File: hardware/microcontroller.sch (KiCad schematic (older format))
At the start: 13 parts, among them U8 STM32F411CEUx, Y1 12MHz

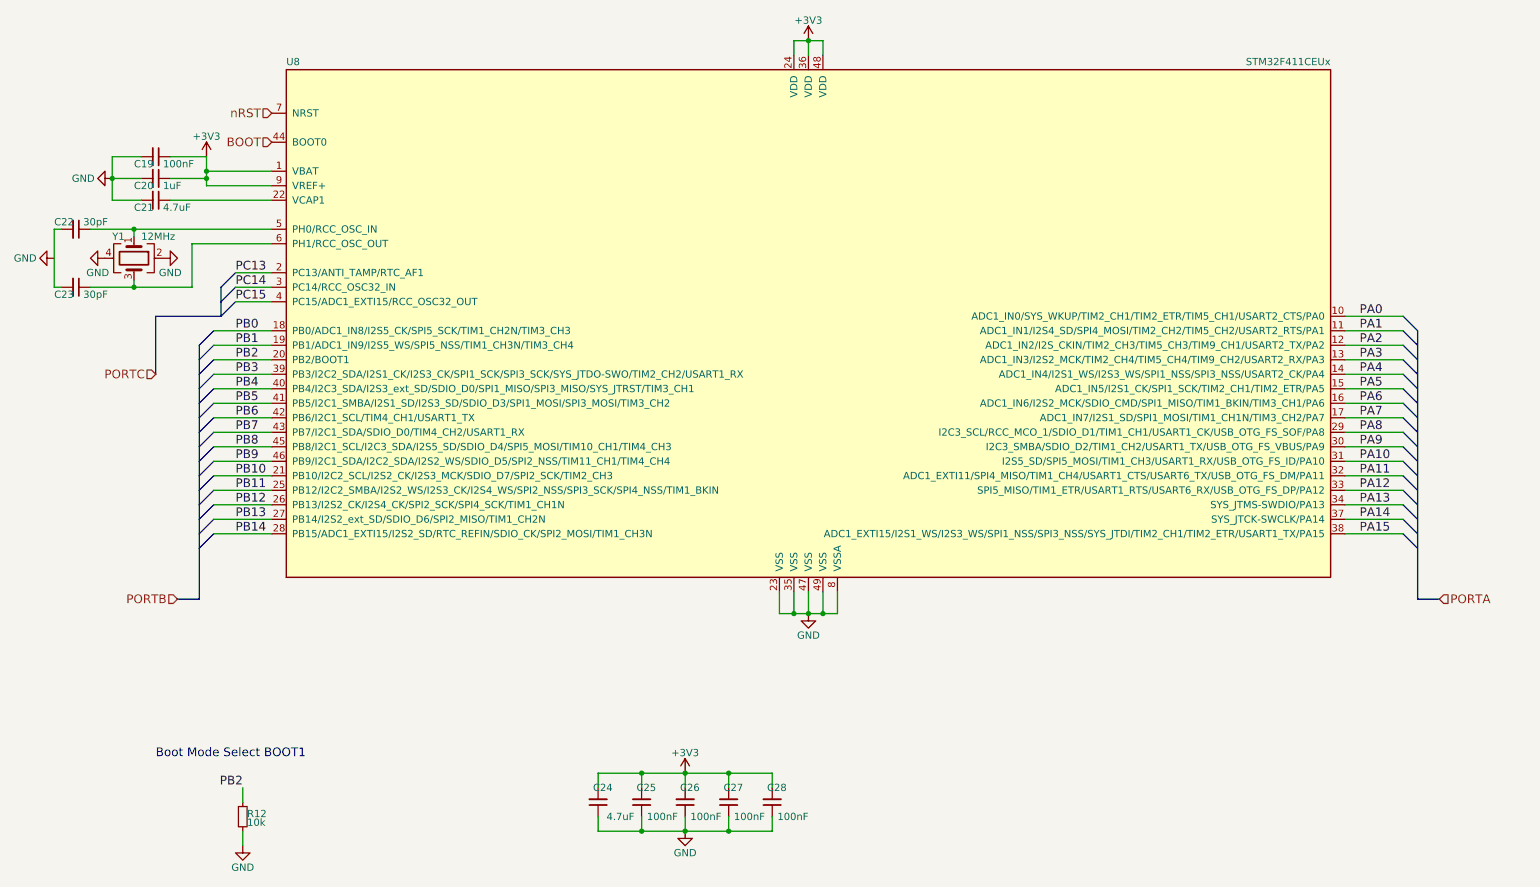
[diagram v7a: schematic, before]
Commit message: Start laying out the components for the PCB
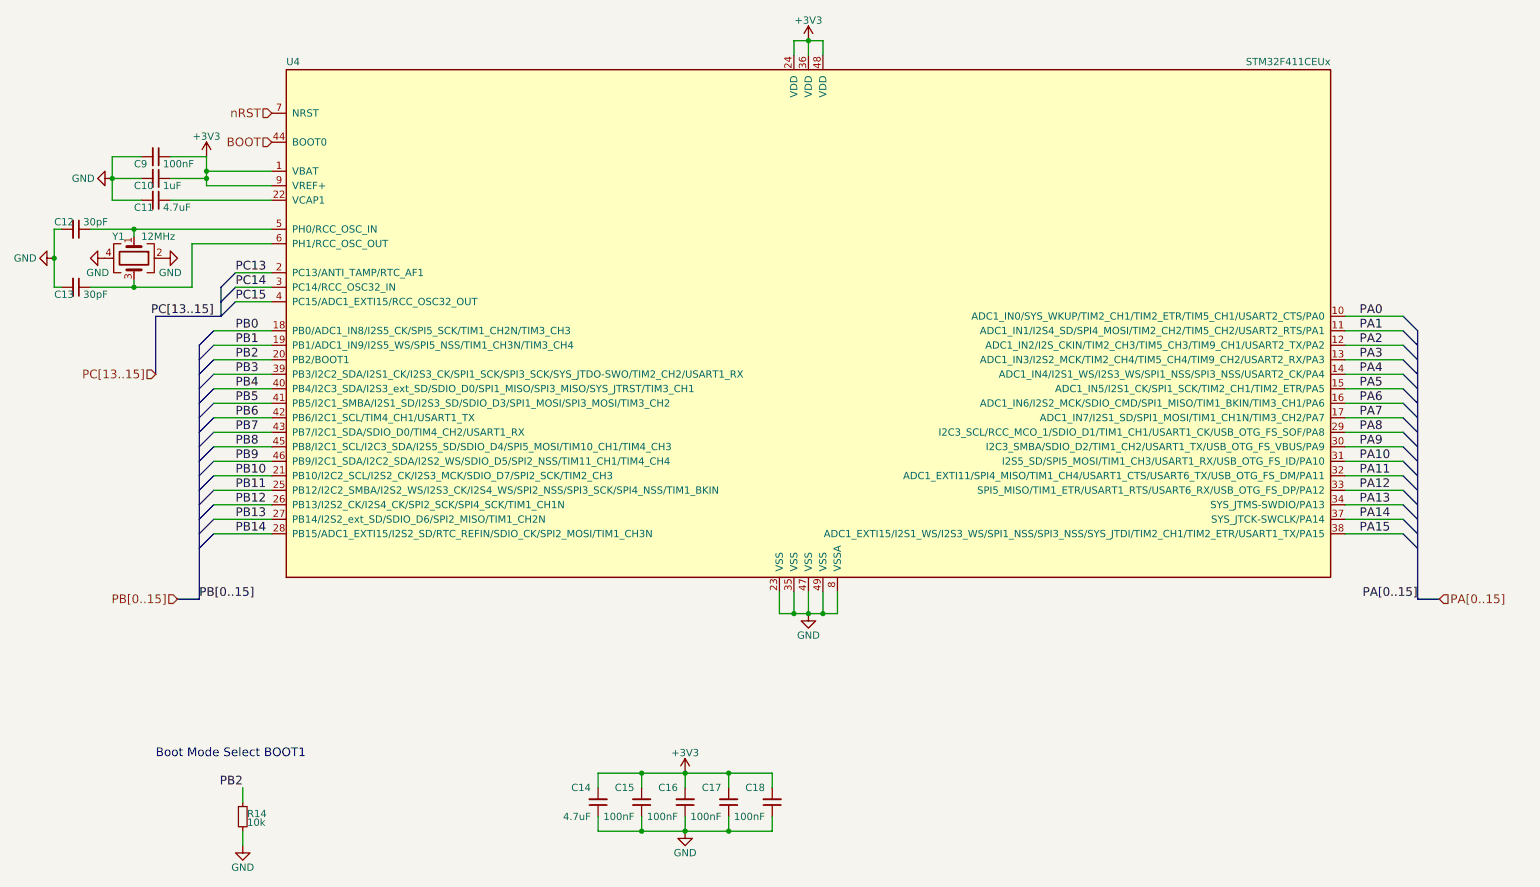
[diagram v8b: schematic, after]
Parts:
- Y1: footprint Crystals:Crystal_SMD_2520-4pin_2.5x2.0mm -> Crystals:Crystal_SMD_3225-4pin_3.2x2.5mm
- renumbered C20 to C10, C21 to C11, C22 to C12, C23 to C13, C24 to C14, C25 to C15, C26 to C16, C27 to C17, C28 to C18, C19 to C9, R12 to R14, U8 to U4
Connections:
- net labels added: PA[0..15], PB[0..15], PC[13..15]
- net labels removed: PORTA, PORTB, PORTC
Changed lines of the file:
@@
 encoding utf-8
 Sheet 2 2
-Title ""
-Date ""
-Rev ""
+Title "MiniBot"
+Date "2017-06-23"
+Rev "1"
 Comp ""
-Comment1 ""
+Comment1 "Ben Mitchell"
 Comment2 ""
 Comment3 ""
@@
 P 6000 3400
 AR Path="/59427B10" Ref="U?"  Part="1"
-AR Path="/59425D39/59427B10" Ref="U8"  Part="1"
-F 0 "U8" H 2400 5225 50  0000 L BNN
+AR Path="/59425D39/59427B10" Ref="U4"  Part="1"
+F 0 "U4" H 2400 5225 50  0000 L BNN
 F 1 "STM32F411CEUx" H 9600 5225 50  0000 R BNN
 F 2 "Housings_DFN_QFN:QFN-48-1EP_7x7mm_Pitch0.5mm" H 9600 5175 50  0001 R TNN
@@
 $EndComp
 $Comp
-L C_Small C21
+L C_Small C11
 U 1 1 59427B23
 P 1500 2500
-F 0 "C21" V 1550 2350 50  0000 L CNN
+F 0 "C11" V 1550 2350 50  0000 L CNN
 F 1 "4.7uF" V 1550 2550 50  0000 L CNN
 F 2 "Capacitors_SMD:C_0805" H 1500 2500 50  0001 C CNN
@@
 $EndComp
 $Comp
-L GND #PWR65
+L GND #PWR040
 U 1 1 59427B2A
 P 1200 2350
-F 0 "#PWR65" H 1200 2100 50  0001 C CNN
+F 0 "#PWR040" H 1200 2100 50  0001 C CNN
 F 1 "GND" V 1200 2150 50  0000 C CNN
 F 2 "" H 1200 2350 50  0001 C CNN
@@
 $EndComp
 $Comp
-L GND #PWR69
+L GND #PWR041
 U 1 1 59427B30
 P 6000 5350
-F 0 "#PWR69" H 6000 5100 50  0001 C CNN
+F 0 "#PWR041" H 6000 5100 50  0001 C CNN
 F 1 "GND" H 6000 5200 50  0000 C CNN
 F 2 "" H 6000 5350 50  0001 C CNN
@@
 $EndComp
 $Comp
-L C_Small C20
+L C_Small C10
 U 1 1 59427B36
 P 1500 2350
-F 0 "C20" V 1550 2200 50  0000 L CNN
+F 0 "C10" V 1550 2200 50  0000 L CNN
 F 1 "1uF" V 1550 2400 50  0000 L CNN
 F 2 "Capacitors_SMD:C_0805" H 1500 2350 50  0001 C CNN
@@
 $EndComp
 $Comp
-L C_Small C19
+L C_Small C9
 U 1 1 59427B3D
 P 1500 2200
-F 0 "C19" V 1550 2050 50  0000 L CNN
+F 0 "C9" V 1550 2050 50  0000 L CNN
 F 1 "100nF" V 1550 2250 50  0000 L CNN
 F 2 "Capacitors_SMD:C_0603" H 1500 2200 50  0001 C CNN
@@
 $EndComp
 $Comp
-L C_Small C25
+L C_Small C15
 U 1 1 59427B44
 P 4850 6650
-F 0 "C25" H 4750 6550 50  0000 L CNN
-F 1 "100nF" H 4600 6750 50  0000 L CNN
+F 0 "C15" H 4900 6550 50  0000 L CNN
+F 1 "100nF" H 4900 6750 50  0000 L CNN
 F 2 "Capacitors_SMD:C_0603" H 4850 6650 50  0001 C CNN
 F 3 "" H 4850 6650 50  0001 C CNN
@@
 $EndComp
 $Comp
-L C_Small C26
+L C_Small C16
 U 1 1 59427B4B
 P 5150 6650
-F 0 "C26" H 5050 6550 50  0000 L CNN
-F 1 "100nF" H 4900 6750 50  0000 L CNN
+F 0 "C16" H 5200 6550 50  0000 L CNN
+F 1 "100nF" H 5200 6750 50  0000 L CNN
 F 2 "Capacitors_SMD:C_0603" H 5150 6650 50  0001 C CNN
 F 3 "" H 5150 6650 50  0001 C CNN
@@
 $EndComp
 $Comp
-L C_Small C27
+L C_Small C17
 U 1 1 59427B52
 P 5450 6650
-F 0 "C27" H 5350 6550 50  0000 L CNN
-F 1 "100nF" H 5200 6750 50  0000 L CNN
+F 0 "C17" H 5500 6550 50  0000 L CNN
+F 1 "100nF" H 5500 6750 50  0000 L CNN
 F 2 "Capacitors_SMD:C_0603" H 5450 6650 50  0001 C CNN
 F 3 "" H 5450 6650 50  0001 C CNN
@@
 $EndComp
 $Comp
-L C_Small C28
+L C_Small C18
 U 1 1 59427B59
 P 5750 6650
-F 0 "C28" H 5650 6550 50  0000 L CNN
-F 1 "100nF" H 5500 6750 50  0000 L CNN
+F 0 "C18" H 5800 6550 50  0000 L CNN
+F 1 "100nF" H 5800 6750 50  0000 L CNN
 F 2 "Capacitors_SMD:C_0603" H 5750 6650 50  0001 C CNN
 F 3 "" H 5750 6650 50  0001 C CNN
@@
 $EndComp
 $Comp
-L GND #PWR71
+L GND #PWR042
 U 1 1 59427B60
 P 5150 6850
-F 0 "#PWR71" H 5150 6600 50  0001 C CNN
+F 0 "#PWR042" H 5150 6600 50  0001 C CNN
 F 1 "GND" H 5150 6700 50  0000 C CNN
 F 2 "" H 5150 6850 50  0001 C CNN
@@
 $EndComp
 $Comp
-L C_Small C24
+L C_Small C14
 U 1 1 59427B6C
 P 4550 6650
-F 0 "C24" H 4450 6550 50  0000 L CNN
-F 1 "4.7uF" H 4300 6750 50  0000 L CNN
+F 0 "C14" H 4600 6550 50  0000 L CNN
+F 1 "4.7uF" H 4600 6750 50  0000 L CNN
 F 2 "Capacitors_SMD:C_0805" H 4550 6650 50  0001 C CNN
 F 3 "" H 4550 6650 50  0001 C CNN
@@
 F 0 "Y1" V 1200 2750 50  0000 L CNN
 F 1 "12MHz" V 1200 2950 50  0000 L CNN
-F 2 "Crystals:Crystal_SMD_2520-4pin_2.5x2.0mm" H 1350 2900 50  0001 C CNN
+F 2 "Crystals:Crystal_SMD_3225-4pin_3.2x2.5mm" H 1350 2900 50  0001 C CNN
 F 3 "" H 1350 2900 50  0001 C CNN
 	1    1350 2900
@@
 Connection ~ 1350 3100
 $Comp
-L GND #PWR67
+L GND #PWR043
 U 1 1 59427C13
 P 1150 2900
-F 0 "#PWR67" H 1150 2650 50  0001 C CNN
+F 0 "#PWR043" H 1150 2650 50  0001 C CNN
 F 1 "GND" V 1250 2850 50  0000 C CNN
 F 2 "" H 1150 2900 50  0001 C CNN
@@
 $EndComp
 $Comp
-L GND #PWR68
+L GND #PWR044
 U 1 1 59427C19
 P 1550 2900
-F 0 "#PWR68" H 1550 2650 50  0001 C CNN
+F 0 "#PWR044" H 1550 2650 50  0001 C CNN
 F 1 "GND" V 1450 2850 50  0000 C CNN
 F 2 "" H 1550 2900 50  0001 C CNN
@@
 $EndComp
 $Comp
-L C_Small C23
+L C_Small C13
 U 1 1 59427C1F
 P 950 3100
-F 0 "C23" V 1000 2950 50  0000 L CNN
+F 0 "C13" V 1000 2950 50  0000 L CNN
 F 1 "30pF" V 1000 3150 50  0000 L CNN
 F 2 "Capacitors_SMD:C_0402" H 950 3100 50  0001 C CNN
@@
 	1750 3100 1050 3100
 $Comp
-L C_Small C22
+L C_Small C12
 U 1 1 59427C28
 P 950 2700
-F 0 "C22" V 900 2550 50  0000 L CNN
+F 0 "C12" V 900 2550 50  0000 L CNN
 F 1 "30pF" V 900 2750 50  0000 L CNN
 F 2 "Capacitors_SMD:C_0402" H 950 2700 50  0001 C CNN
@@
 	1050 2700 2300 2700
 $Comp
-L GND #PWR66
+L GND #PWR045
 U 1 1 59427C31
 P 800 2900
-F 0 "#PWR66" H 800 2650 50  0001 C CNN
+F 0 "#PWR045" H 800 2650 50  0001 C CNN
 F 1 "GND" V 800 2700 50  0000 C CNN
 F 2 "" H 800 2900 50  0001 C CNN
@@
 $EndComp
 Text HLabel 10350 5250 2    60   Input ~ 0
-PORTA
+PA[0..15]
 Text HLabel 1650 5250 0    60   Input ~ 0
-PORTB
+PB[0..15]
 Text HLabel 2300 1900 0    60   Input ~ 0
 nRST
@@
 PB2
 $Comp
-L R_Small R12
+L R_Small R14
 U 1 1 594293DA
 P 2100 6750
-F 0 "R12" H 2130 6770 50  0000 L CNN
+F 0 "R14" H 2130 6770 50  0000 L CNN
 F 1 "10k" H 2130 6710 50  0000 L CNN
 F 2 "Resistors_SMD:R_0603" H 2100 6750 50  0001 C CNN
@@
 $EndComp
 $Comp
-L GND #PWR72
+L GND #PWR046
 U 1 1 5942944C
 P 2100 6950
-F 0 "#PWR72" H 2100 6700 50  0001 C CNN
+F 0 "#PWR046" H 2100 6700 50  0001 C CNN
 F 1 "GND" H 2100 6800 50  0000 C CNN
 F 2 "" H 2100 6950 50  0001 C CNN
@@
 	1500 3300 1500 3700
 Text HLabel 1500 3700 0    60   Input ~ 0
-PORTC
-$Comp
-L +3V3 #PWR63
+PC[13..15]
+$Comp
+L +3V3 #PWR047
 U 1 1 59492047
 P 6000 1400
-F 0 "#PWR63" H 6000 1250 50  0001 C CNN
+F 0 "#PWR047" H 6000 1250 50  0001 C CNN
 F 1 "+3V3" H 6000 1540 50  0000 C CNN
 F 2 "" H 6000 1400 50  0001 C CNN
@@
 $EndComp
 $Comp
-L +3V3 #PWR70
+L +3V3 #PWR048
 U 1 1 59492080
 P 5150 6450
-F 0 "#PWR70" H 5150 6300 50  0001 C CNN
+F 0 "#PWR048" H 5150 6300 50  0001 C CNN
 F 1 "+3V3" H 5150 6590 50  0000 C CNN
 F 2 "" H 5150 6450 50  0001 C CNN
@@
 $EndComp
 $Comp
-L +3V3 #PWR64
+L +3V3 #PWR049
 U 1 1 594920B2
 P 1850 2200
-F 0 "#PWR64" H 1850 2050 50  0001 C CNN
+F 0 "#PWR049" H 1850 2050 50  0001 C CNN
 F 1 "+3V3" H 1850 2340 50  0000 C CNN
 F 2 "" H 1850 2200 50  0001 C CNN
@@
 	1    0    0    -1
 $EndComp
+Connection ~ 800  2900
+Text Label 1900 3300 2    60   ~ 0
+PC[13..15]
+Text Label 1800 5250 0    60   ~ 0
+PB[0..15]
+Text Label 10200 5250 2    60   ~ 0
+PA[0..15]
 $EndSCHEMATC
